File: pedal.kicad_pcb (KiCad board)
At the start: 4 copper layers, 68 parts, among them J2 USB_C_Receptacle_USB2.0_16P, J3 VBATT, J4 THERM, J5 GND, J6 GND, SW1 MK-11C04-G013, U1 STM32H745XIH6, U2 TPS631000DRLR, U3 TLV77018PDBVR, U4 TPS2116DRL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

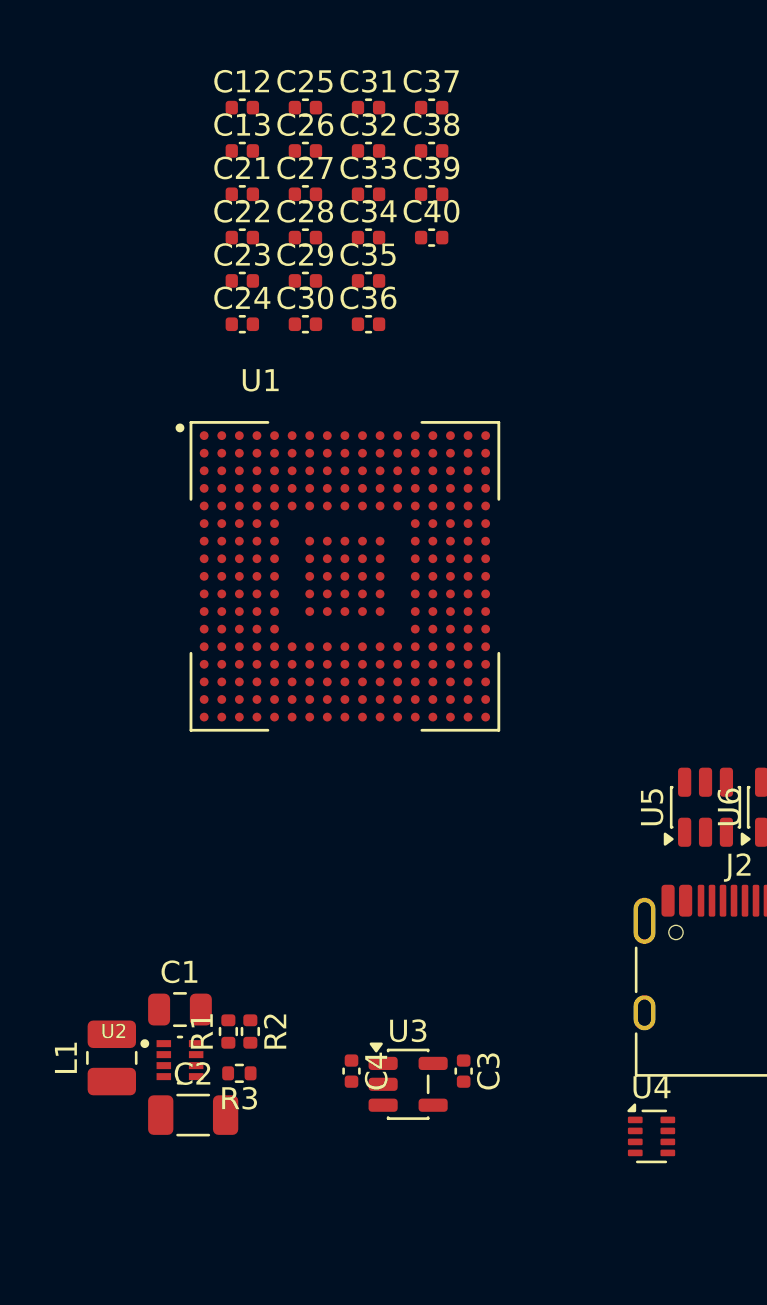
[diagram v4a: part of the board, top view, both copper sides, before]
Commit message: fix footprints and add smps
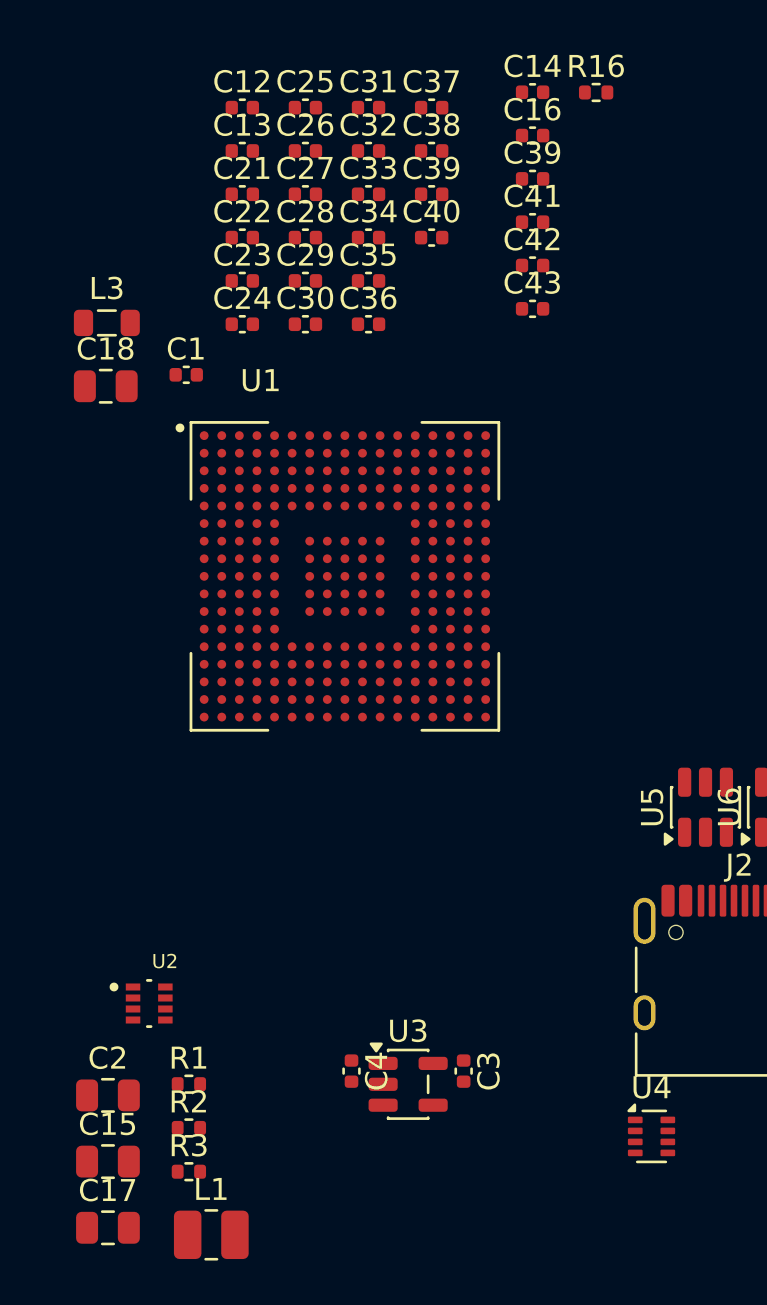
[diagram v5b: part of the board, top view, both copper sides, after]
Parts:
- added C14: 4.7uF, Capacitor_SMD:C_0402_1005Metric, F.Cu at (133.2, 91.3)
- added C15: 22uF, Capacitor_SMD:C_0805_2012Metric, F.Cu at (113.9, 139.9)
- added C16: 10nF, Capacitor_SMD:C_0402_1005Metric, F.Cu at (133.2, 93.3)
- added C17: 22uF, Capacitor_SMD:C_0805_2012Metric, F.Cu at (113.9, 142.9)
- added C18: 22uF, Capacitor_SMD:C_0805_2012Metric, F.Cu at (113.8, 104.7)
- added C39: 1uF, Capacitor_SMD:C_0402_1005Metric, F.Cu at (133.2, 95.2)
- added C41: 1uF, Capacitor_SMD:C_0402_1005Metric, F.Cu at (133.2, 97.2)
- added C42: 1uF, Capacitor_SMD:C_0402_1005Metric, F.Cu at (133.2, 99.2)
- added C43: 1uF, Capacitor_SMD:C_0402_1005Metric, F.Cu at (133.2, 101.1)
- added L3: 2.2uH, Inductor_SMD:L_0805_2012Metric, F.Cu at (113.9, 101.8)
- added R16: 10k, Resistor_SMD:R_0402_1005Metric, F.Cu at (136.1, 91.3)
- C1: value 47uF -> 220pF; footprint Capacitor_SMD:C_0805_2012Metric -> Capacitor_SMD:C_0402_1005Metric
- C2: footprint Capacitor_SMD:C_1206_3216Metric -> Capacitor_SMD:C_0805_2012Metric
- U1: footprint footprints:BGA265C80P17X17_1400X1400X120 -> custom:BGA265C80P17X17_1400X1400X120
- U2: footprint footprints:SOT50P160X60-8N -> custom:SOT50P160X60-8N
- moved C1 28.9 mm to (117.5, 104.1)
- moved L1 9.23 mm to (118.6, 143.2), turned to 0 degrees
- moved R2 5.20 mm to (117.6, 138.4), turned to 0 degrees
- moved R3 5.03 mm to (117.6, 140.4), turned to 0 degrees
- moved C2 3.98 mm to (113.9, 136.9)
- moved R1 2.99 mm to (117.6, 136.4), turned to 0 degrees
- moved U2 2.93 mm to (115.8, 132.7)
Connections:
- C1 pad 1: +3V3 -> Net-(U1C-VLXSMPS)
- U1 pad A6: +3V3 -> VDDLDO
- U1 pad C17: +3V3 -> VDDLDO
- U1 pad E1: unconnected-(U1C-VLXSMPS-PadE1) -> Net-(U1C-VLXSMPS)
- U1 pad E7: unconnected-(U1B-PDR_ON-PadE7) -> +3V3
- U1 pad E8: unconnected-(U1B-BOOT0-PadE8) -> Net-(U1B-BOOT0)
- U1 pad F1: unconnected-(U1C-VDDSMPS-PadF1) -> +3V3
- U1 pad F2: unconnected-(U1C-VSSSMPS-PadF2) -> GND
- U1 pad G17: unconnected-(U1C-VDD50USB-PadG17) -> +3V3
- U1 pad G2: unconnected-(U1C-VFBSMPS-PadG2) -> VDDLDO
- U1 pad K1: unconnected-(U1B-~{RST}-PadK1) -> /microcontroller/NRST
- U1 pad U12: +3V3 -> VDDLDO

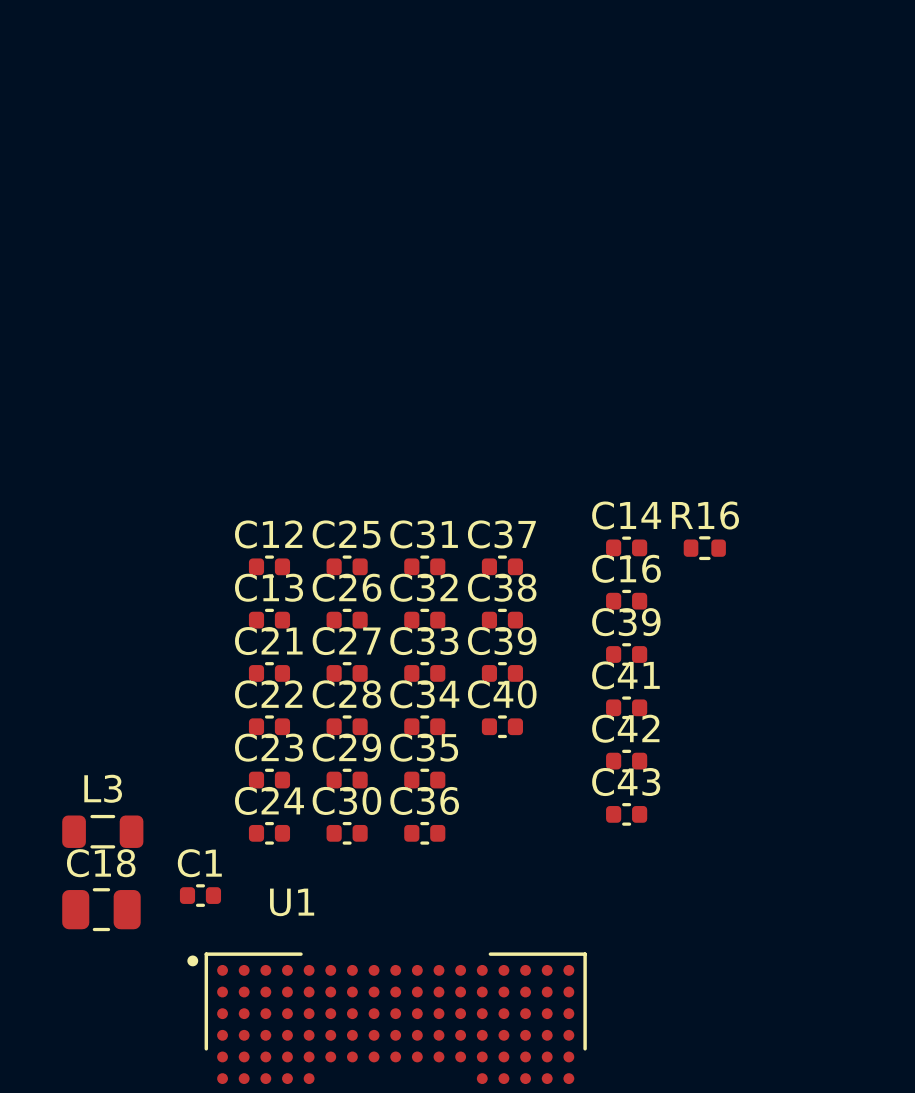
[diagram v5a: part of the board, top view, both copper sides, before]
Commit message: add all external signals
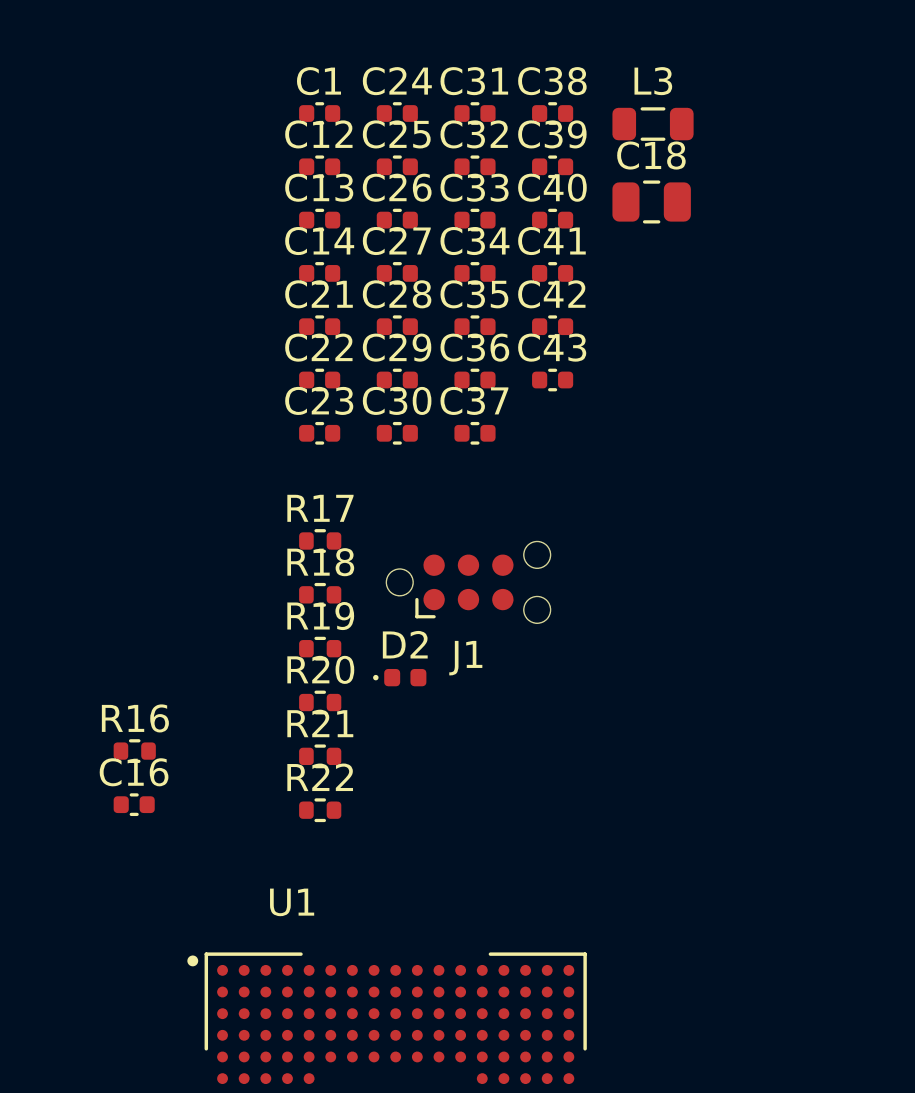
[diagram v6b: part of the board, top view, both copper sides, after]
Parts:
- removed the C39 at (128.6, 95.9)
- removed the C39 at (133.2, 95.2)
- added C39: 1uF, Capacitor_SMD:C_0402_1005Metric, F.Cu at (130.5, 77.2)
- added D2: LED, LED_SMD:LED_0402_1005Metric, F.Cu at (125.1, 96.1)
- added J1: TagConnect, Connector:Tag-Connect_TC2030-IDC-NL_2x03_P1.27mm_Vertical, F.Cu at (127.4, 92.6)
- added R17: 15k, Resistor_SMD:R_0402_1005Metric, F.Cu at (121.9, 91.0)
- added R18: 10k, Resistor_SMD:R_0402_1005Metric, F.Cu at (121.9, 93.0)
- added R19: 4.7k, Resistor_SMD:R_0402_1005Metric, F.Cu at (121.9, 95.0)
- added R20: 4.7k, Resistor_SMD:R_0402_1005Metric, F.Cu at (121.9, 97.0)
- added R21: 4.7k, Resistor_SMD:R_0402_1005Metric, F.Cu at (121.9, 99.0)
- added R22: 4.7k, Resistor_SMD:R_0402_1005Metric, F.Cu at (121.9, 101.0)
- moved L3 33.1 mm to (134.2, 75.6)
- moved C18 33.1 mm to (134.2, 78.5)
- moved C1 29.2 mm to (121.9, 75.2)
- moved C24 27.0 mm to (124.8, 75.2)
- moved R16 22.4 mm to (115.1, 98.8)
- moved C16 19.7 mm to (115.0, 100.8)
- moved C38 18.8 mm to (130.5, 75.2)
- moved C40 18.8 mm to (130.5, 79.2)
- moved C31 16.9 mm to (127.6, 75.2)
- moved C32 16.9 mm to (127.6, 77.2)
- moved C33 16.9 mm to (127.6, 79.2)
- moved C34 16.9 mm to (127.6, 81.1)
- moved C35 16.9 mm to (127.6, 83.1)
- moved C36 16.9 mm to (127.6, 85.1)
- moved C42 16.3 mm to (130.5, 83.1)
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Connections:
- J2 pad A6: /Power path/D+ -> /Power path/USB.D+
- J2 pad A7: /Power path/D- -> /Power path/USB.D-
- J2 pad A8: /Power path/SBU1 -> /Power path/SBU.TX
- J2 pad B6: /Power path/D+ -> /Power path/USB.D+
- J2 pad B7: /Power path/D- -> /Power path/USB.D-
- J2 pad B8: /Power path/SBU2 -> /Power path/SBU.RX
- U1 pad A10: unconnected-(U1B-PG9-PadA10) -> /microcontroller/IMU.CIPO
- U1 pad A11: unconnected-(U1A-PD5-PadA11) -> /microcontroller/LCD.WR
- U1 pad A12: unconnected-(U1A-PD4-PadA12) -> /microcontroller/LCD.RD
- U1 pad A13: unconnected-(U1A-PC10-PadA13) -> /microcontroller/PEDAL.TX
- U1 pad A15: unconnected-(U1B-PI1-PadA15) -> /microcontroller/PS_MODE
- U1 pad A16: unconnected-(U1B-PI0-PadA16) -> /microcontroller/IMU_FSYNC
- U1 pad A4: unconnected-(U1B-PI4-PadA4) -> /microcontroller/LCD.nRST
- U1 pad A5: unconnected-(U1A-PB5-PadA5) -> /microcontroller/IMU.COPI
- U1 pad A9: unconnected-(U1B-PG10-PadA9) -> /microcontroller/IMU.nCS
- U1 pad B11: unconnected-(U1A-PD6-PadB11) -> /microcontroller/CODEC.SDO
- U1 pad B13: unconnected-(U1A-PC11-PadB13) -> /microcontroller/PEDAL.RX
- U1 pad B14: unconnected-(U1A-PA14(JTCK/SWCLK)-PadB14) -> /microcontroller/SWCLK
- U1 pad B15: unconnected-(U1B-PI2-PadB15) -> /microcontroller/CHARGER_nEN
- U1 pad B5: unconnected-(U1A-PB6-PadB5) -> /microcontroller/FUEL_GAUGE.SCL
- U1 pad B9: unconnected-(U1B-PG11-PadB9) -> /microcontroller/IMU.SCK
- U1 pad C11: unconnected-(U1A-PD7-PadC11) -> /microcontroller/LCD.nCS
- U1 pad C14: unconnected-(U1B-PI3-PadC14) -> /microcontroller/CHARGER_ICHG
- U1 pad C15: unconnected-(U1A-PA13(JTMS/SWDIO)-PadC15) -> /microcontroller/SWDIO
- U1 pad C4: unconnected-(U1A-PE0-PadC4) -> /microcontroller/LCD.TE
- U1 pad C5: unconnected-(U1A-PB7-PadC5) -> /microcontroller/FUEL_GAUGE.SDA
- U1 pad C6: unconnected-(U1A-PB3(JTDO/TRACESWO)-PadC6) -> /microcontroller/SWO
- U1 pad D1: unconnected-(U1A-PE5-PadD1) -> /microcontroller/CODEC.SCK
- U1 pad D13: unconnected-(U1A-PD0-PadD13) -> /microcontroller/LCD.DB2
- U1 pad D2: unconnected-(U1A-PE4-PadD2) -> /microcontroller/CODEC.WS
- U1 pad D3: unconnected-(U1A-PE3-PadD3) -> /microcontroller/CODEC.SDI
- U1 pad E12: unconnected-(U1A-PD1-PadE12) -> /microcontroller/LCD.DB3
- U1 pad E16: unconnected-(U1A-PA12-PadE16) -> /microcontroller/USB.D+
- U1 pad E17: unconnected-(U1A-PA11-PadE17) -> /microcontroller/USB.D-
- U1 pad G3: unconnected-(U1A-PF1-PadG3) -> /microcontroller/CODEC.SCL
- U1 pad G4: unconnected-(U1A-PF0-PadG4) -> /microcontroller/LCD.DC
- U1 pad K14: unconnected-(U1B-PJ11-PadK14) -> /microcontroller/IMU_INT
- U1 pad L14: unconnected-(U1B-PJ10-PadL14) -> /microcontroller/CHARGER_STAT
- U1 pad M14: unconnected-(U1B-PJ9-PadM14) -> /microcontroller/PS_MUX
- U1 pad N13: unconnected-(U1B-PJ8-PadN13) -> /microcontroller/FUEL_GAUGE_INT
- U1 pad N14: unconnected-(U1B-PJ7-PadN14) -> /microcontroller/INPUT.L
- U1 pad N15: unconnected-(U1B-PJ6-PadN15) -> /microcontroller/INPUT.R
- U1 pad N6: unconnected-(U1B-PJ0-PadN6) -> /microcontroller/INPUT.A
- U1 pad N9: unconnected-(U1A-PE10-PadN9) -> /microcontroller/LCD.DB7
- U1 pad P10: unconnected-(U1A-PE11-PadP10) -> /microcontroller/LCD.DB8
- U1 pad P15: unconnected-(U1A-PD15-PadP15) -> /microcontroller/LCD.DB1
- U1 pad P16: unconnected-(U1A-PD14-PadP16) -> /microcontroller/LCD.DB0
- U1 pad P4: unconnected-(U1B-PH5-PadP4) -> /microcontroller/CODEC.SDA
- U1 pad P6: unconnected-(U1B-PJ1-PadP6) -> /microcontroller/INPUT.B
- U1 pad P9: unconnected-(U1A-PE9-PadP9) -> /microcontroller/LCD.DB6
- U1 pad R10: unconnected-(U1A-PE12-PadR10) -> /microcontroller/LCD.DB9
- U1 pad R11: unconnected-(U1A-PE15-PadR11) -> /microcontroller/LCD.DB12
- U1 pad R12: unconnected-(U1B-PJ5-PadR12) -> /microcontroller/INPUT.SELECT
- U1 pad T10: unconnected-(U1A-PE13-PadT10) -> /microcontroller/LCD.DB10
- U1 pad T16: unconnected-(U1A-PD10-PadT16) -> /microcontroller/LCD.DB15
- U1 pad T17: unconnected-(U1A-PD9-PadT17) -> /microcontroller/LCD.DB14
- U1 pad T3: unconnected-(U1A-PA5-PadT3) -> /microcontroller/USER_LED
- U1 pad T6: unconnected-(U1B-PJ2-PadT6) -> /microcontroller/INPUT.X
- U1 pad T9: unconnected-(U1A-PE8-PadT9) -> /microcontroller/LCD.DB5
- U1 pad U10: unconnected-(U1A-PE14-PadU10) -> /microcontroller/LCD.DB11
- U1 pad U16: unconnected-(U1A-PD8-PadU16) -> /microcontroller/LCD.DB13
- U1 pad U2: unconnected-(U1A-PA3-PadU2) -> /microcontroller/INPUT.STICK_X
- U1 pad U3: unconnected-(U1A-PA4-PadU3) -> /microcontroller/INPUT.STICK_Y
- U1 pad U6: unconnected-(U1B-PJ3-PadU6) -> /microcontroller/INPUT.Y
- U1 pad U7: unconnected-(U1B-PJ4-PadU7) -> /microcontroller/INPUT.START
- U1 pad U9: unconnected-(U1A-PE7-PadU9) -> /microcontroller/LCD.DB4
